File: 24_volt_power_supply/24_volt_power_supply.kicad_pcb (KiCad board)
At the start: 2 copper layers, 75 x 50 mm, 11 parts, among them J1 Conn_01x02_Pin, J2 Screw_Terminal_01x02, J3 Conn_01x02_Pin, K1 Relay_SPDT

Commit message: increased trace thickness for high power
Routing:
- net AC: track 100.7 -> 117.4 mm
- net Net-(J3-Pin_1): track 63.3 -> 65.0 mm
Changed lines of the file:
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@@
 		(start 80.5 71.5)
 		(end 83.5 74.5)
+		(width 3)
+		(layer "F.Cu")
+		(net 3)
+	)
+	(segment
+		(start 92.955113 79.265113)
+		(end 88.19 74.5)
 		(width 0.2)
 		(layer "F.Cu")
@@
 	)
 	(segment
-		(start 125.5 86)
-		(end 130 86)
-		(width 0.2)
-		(layer "F.Cu")
-		(net 3)
-	)
-	(segment
 		(start 87.5 99.5)
 		(end 103.5 99.5)
@@
 	)
 	(segment
-		(start 115 93)
-		(end 118.5 93)
-		(width 0.2)
-		(layer "F.Cu")
-		(net 3)
-	)
-	(segment
 		(start 83.5 95.5)
 		(end 87.5 99.5)
-		(width 0.2)
-		(layer "F.Cu")
-		(net 3)
-	)
-	(segment
-		(start 92.955113 79.265113)
-		(end 88.19 74.5)
-		(width 0.2)
+		(width 3)
 		(layer "F.Cu")
 		(net 3)
@@
 		(start 83.5 74.5)
 		(end 83.5 95.5)
-		(width 0.2)
+		(width 3)
 		(layer "F.Cu")
 		(net 3)
@@
 		(start 103.5 99.5)
 		(end 112.5 90.5)
-		(width 0.2)
-		(layer "F.Cu")
-		(net 3)
-	)
-	(segment
-		(start 118.5 93)
-		(end 125.5 86)
-		(width 0.2)
+		(width 3)
 		(layer "F.Cu")
 		(net 3)
@@
 		(start 76.5 71.5)
 		(end 80.5 71.5)
-		(width 0.2)
+		(width 3)
 		(layer "F.Cu")
 		(net 3)
@@
 	)
 	(segment
-		(start 112.5 90.5)
-		(end 115 93)
-		(width 0.2)
-		(layer "F.Cu")
+		(start 127.5 83.5)
+		(end 130 86)
+		(width 0.2)
+		(layer "B.Cu")
+		(net 3)
+	)
+	(segment
+		(start 92.955113 83.5)
+		(end 127.5 83.5)
+		(width 0.2)
+		(layer "B.Cu")
 		(net 3)
 	)
@@
 		(start 98 80.5)
 		(end 120.5 58)
-		(width 0.2)
+		(width 3)
+		(layer "B.Cu")
+		(net 7)
+	)
+	(segment
+		(start 128.5 56)
+		(end 130.5 58)
+		(width 3)
+		(layer "B.Cu")
+		(net 7)
+	)
+	(segment
+		(start 122.5 56)
+		(end 128.5 56)
+		(width 3)
 		(layer "B.Cu")
 		(net 7)
@@
 	(segment
 		(start 120.5 58)
-		(end 130.5 58)
-		(width 0.2)
+		(end 122.5 56)
+		(width 3)
 		(layer "B.Cu")
 		(net 7)
@@
 		(start 76.5 80.5)
 		(end 98 80.5)
-		(width 0.2)
+		(width 3)
 		(layer "B.Cu")
 		(net 7)
@@
 		(start 132.8 72.2)
 		(end 136.5 72.2)
-		(width 0.2)
+		(width 3)
 		(layer "F.Cu")
 		(net 8)
@@
 		(start 114.5 90.5)
 		(end 132.8 72.2)
-		(width 0.2)
+		(width 3)
 		(layer "F.Cu")
 		(net 8)
@@
 		(start 110.5 89.745)
 		(end 124.5 75.745)
-		(width 0.2)
+		(width 3)
 		(layer "F.Cu")
 		(net 9)
@@
 		(start 124.5 75.745)
 		(end 124.5 72.2)
-		(width 0.2)
+		(width 3)
 		(layer "F.Cu")
 		(net 9)
@@
 		(min_thickness 0.25)
 		(filled_areas_thickness no)
-		(fill yes
+		(fill
 			(thermal_gap 0.5)
 			(thermal_bridge_width 0.5)
@@
 		(polygon
 			(pts
-				(xy 71.5 54.5) (xy 172 54.5) (xy 171.5 154) (xy 71.5 154)
+				(xy 71.5 54.5) (xy 146 55) (xy 146 104.5) (xy 71.5 103.5)
 			)
 		)

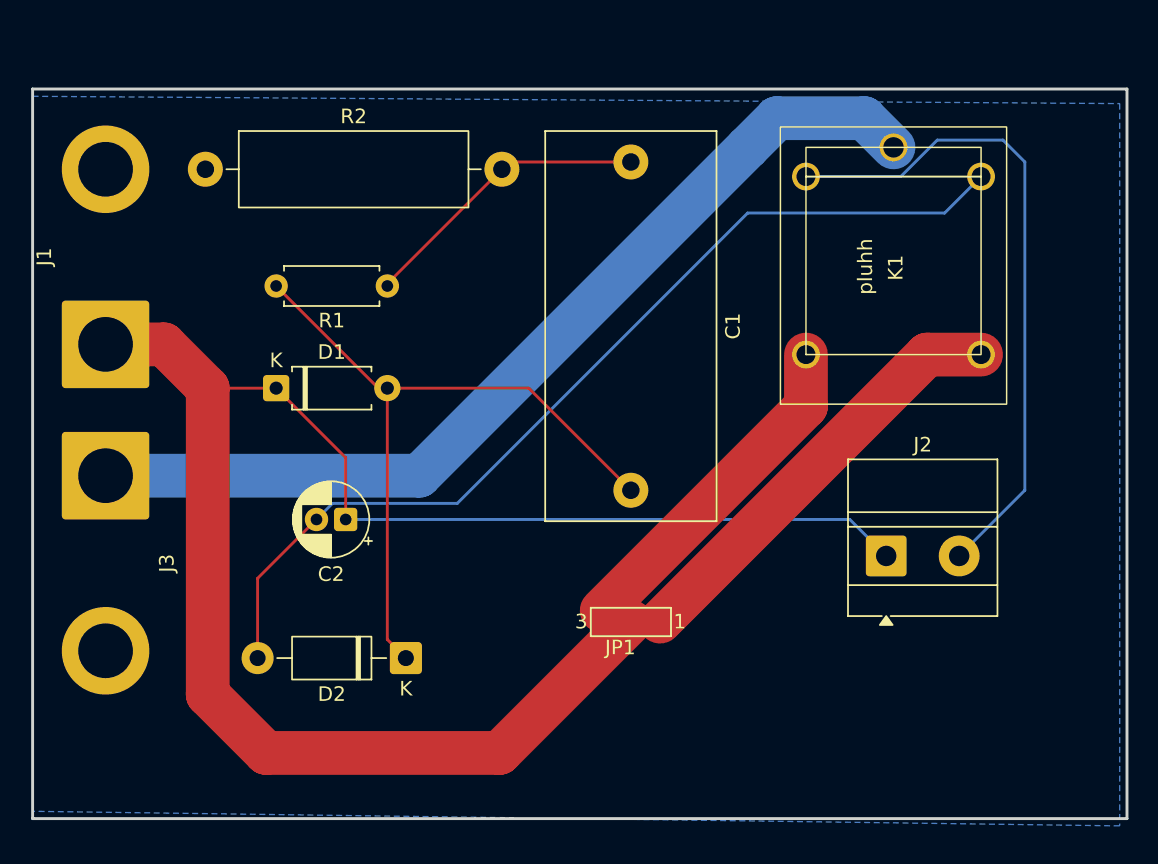
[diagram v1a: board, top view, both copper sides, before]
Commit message: fixed gnd plane issues
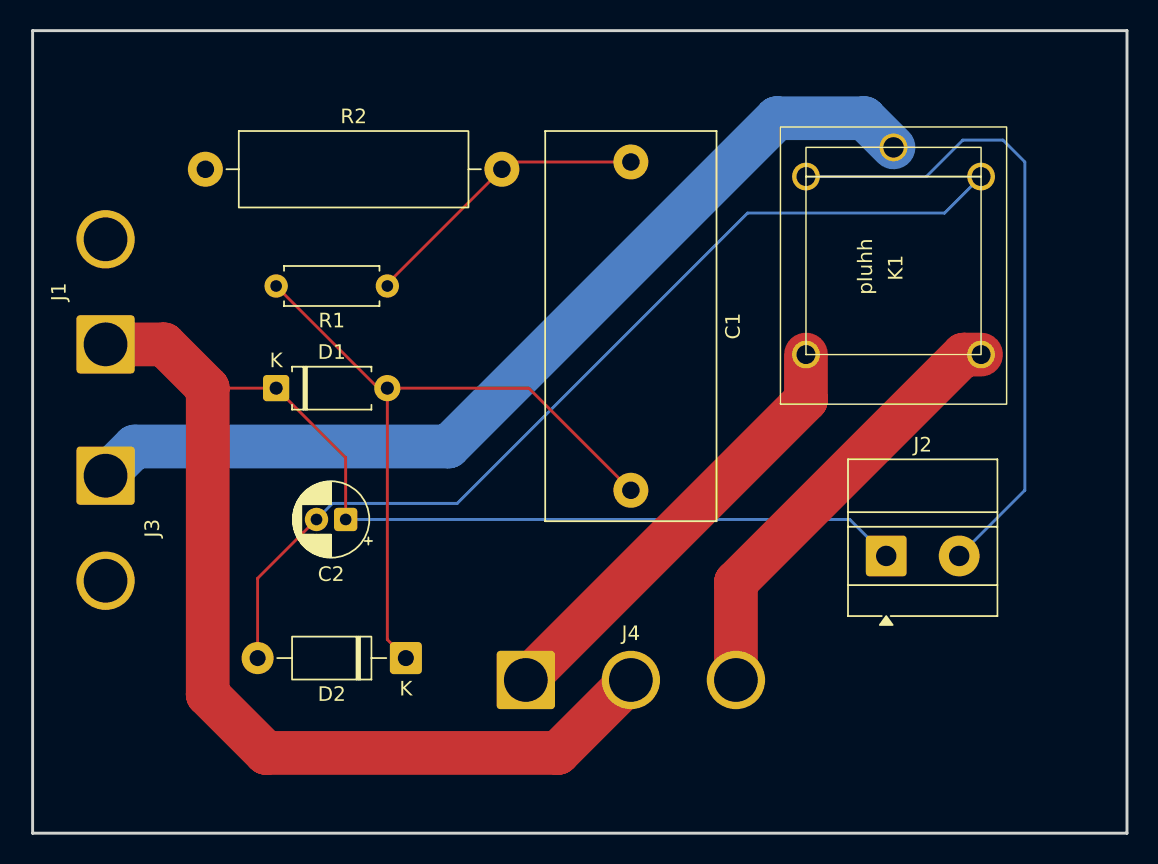
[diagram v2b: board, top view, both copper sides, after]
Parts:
- removed JP1: SolderJumper_3_Open, Jumper:SolderJumper-3_P2.0mm_Open_TrianglePad1.0x1.5mm_NumberLabels
- added J4: Conn_01x03_Pin, Connector_Wire:SolderWire-2.5sqmm_1x03_P7.2mm_D2.4mm_OD3.6mm, F.Cu at (105.3, 94.5)
- J1, J3: footprint Connector_Wire:SolderWire-4sqmm_1x02_P12mm_D3mm_OD6mm -> Connector_Wire:SolderWire-2.5sqmm_1x02_P7.2mm_D2.4mm_OD3.6mm
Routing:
- net Net-(J4-Pin_1): track 24.1 -> 30.3 mm
- net AC: track 117.4 -> 115.7 mm
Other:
- board size 75 x 50 mm -> 75 x 55 mm

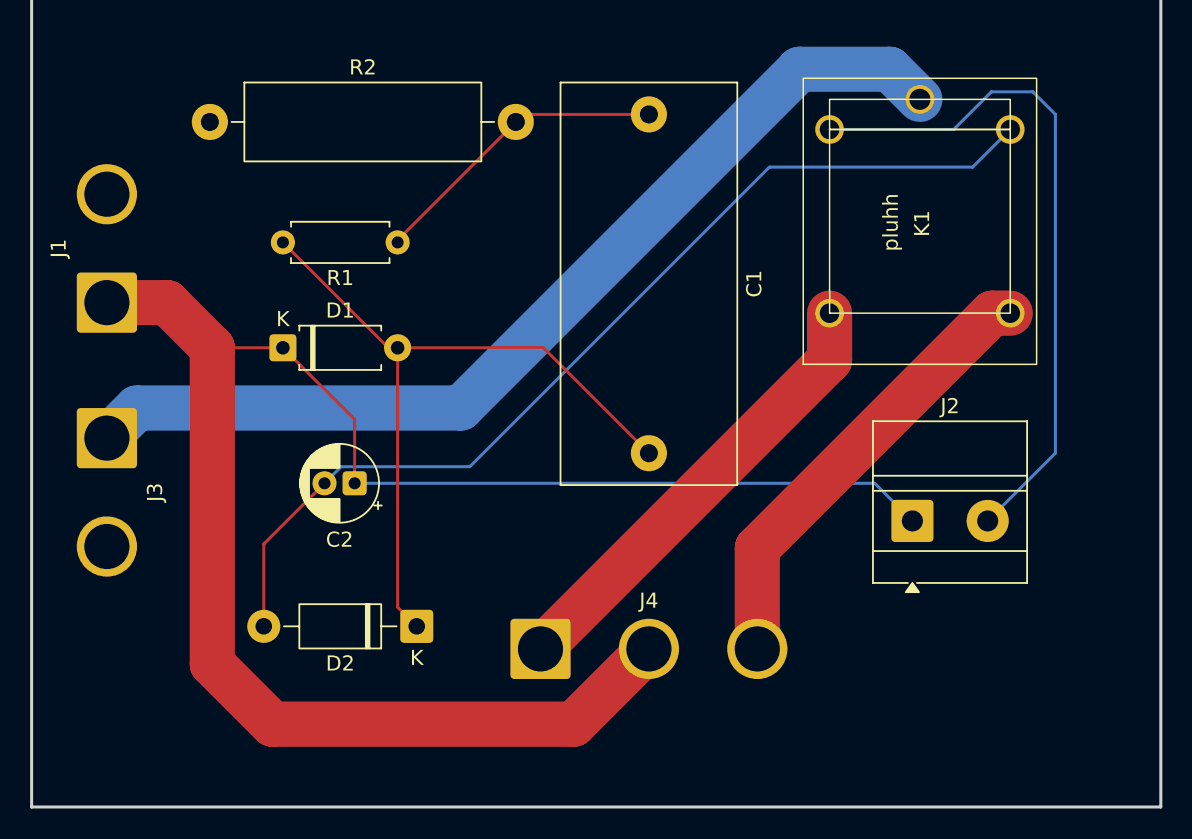
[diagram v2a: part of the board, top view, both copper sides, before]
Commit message: added freewheeling diode
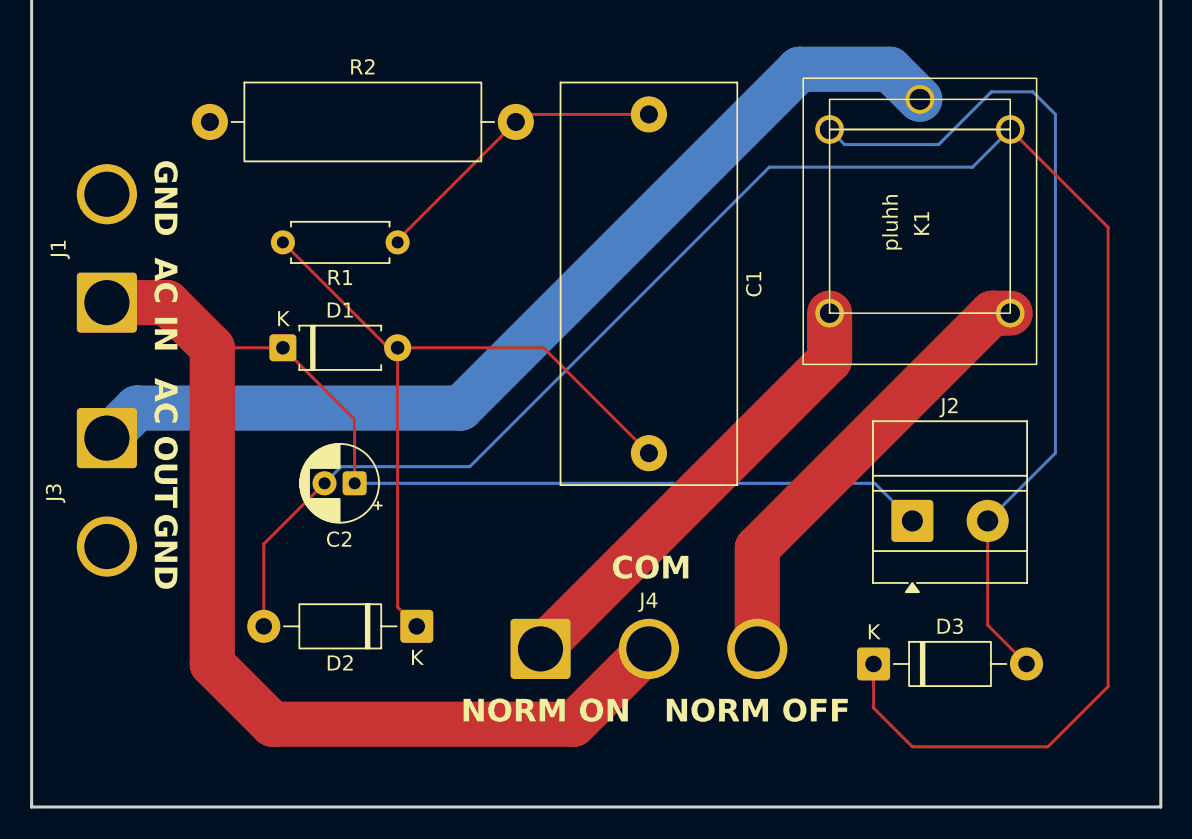
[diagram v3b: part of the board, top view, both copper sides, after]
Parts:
- added D3: 1N4003, Diode_THT:D_DO-41_SOD81_P10.16mm_Horizontal, F.Cu at (127.4, 95.5)
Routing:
- net Net-(D2-A): track 66.5 -> 127.4 mm
- net Net-(D3-A): track 45.5 -> 56.9 mm
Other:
- board text added: "AC IN"
- board text added: "AC OUT"
- board text added: "COM"
- board text added: "GND"
- board text added: "NORM OFF"
- board text added: "NORM ON"

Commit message: updated pcb
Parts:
- moved D3 10.1 mm to (137.5, 95.5), turned to 180 degrees
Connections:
- D3 pad 1: Net-(D2-A) -> Net-(D3-K)
- D3 pad 2: Net-(D3-A) -> Net-(D2-A)
- J2 pad 2: Net-(D3-A) -> Net-(D3-K)
- K1 pad A1: Net-(D3-A) -> Net-(D3-K)
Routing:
- net Net-(D3-K): track 0.00 -> 56.9 mm
- net Net-(D3-A): track 56.9 -> 0.00 mm
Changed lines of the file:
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@@
 	(net 4 "Net-(D2-A)")
 	(net 5 "GND")
-	(net 6 "Net-(D3-A)")
+	(net 6 "Net-(D3-K)")
 	(net 7 "Net-(J3-Pin_1)")
 	(net 8 "Net-(J4-Pin_3)")
@@
 			(layers "*.Cu" "*.Mask")
 			(remove_unused_layers no)
-			(net 6 "Net-(D3-A)")
+			(net 6 "Net-(D3-K)")
 			(pinfunction "Pin_2")
 			(pintype "passive")
@@
 			(layers "*.Cu" "*.Mask")
 			(remove_unused_layers no)
-			(net 6 "Net-(D3-A)")
+			(net 6 "Net-(D3-K)")
 			(pintype "passive")
 		)
@@
 	(footprint "Diode_THT:D_DO-41_SOD81_P10.16mm_Horizontal"
 		(layer "F.Cu")
-		(at 127.42 95.5)
+		(at 137.5 95.5 180)
 		(descr "Diode, DO-41_SOD81 series, Axial, Horizontal, pin pitch=10.16mm, length*diameter=5.2*2.7mm^2, https://www.diodes.com/assets/Package-Files/DO-41-Plastic.pdf")
 		(tags "Diode DO-41_SOD81 series Axial Horizontal pin pitch 10.16mm  length 5.2mm diameter 2.7mm")
@@
 		)
 		(property "Sim.Device" "D"
-			(at 0 0 0)
+			(at 0 0 180)
 			(unlocked yes)
 			(layer "F.Fab")
@@
 		)
 		(property "Sim.Pins" "1=K 2=A"
-			(at 0 0 0)
+			(at 0 0 180)
 			(unlocked yes)
 			(layer "F.Fab")
@@
 		(attr through_hole)
 		(fp_line
-			(start 1.34 0)
-			(end 2.36 0)
+			(start 8.82 0)
+			(end 7.8 0)
 			(stroke
 				(width 0.12)
@@
 		)
 		(fp_line
-			(start 3.14 -1.47)
-			(end 3.14 1.47)
+			(start 3.38 -1.47)
+			(end 3.38 1.47)
 			(stroke
 				(width 0.12)
@@
 		)
 		(fp_line
-			(start 3.38 -1.47)
-			(end 3.38 1.47)
+			(start 3.14 -1.47)
+			(end 3.14 1.47)
 			(stroke
 				(width 0.12)
@@
 		)
 		(fp_line
-			(start 8.82 0)
-			(end 7.8 0)
+			(start 1.34 0)
+			(end 2.36 0)
 			(stroke
 				(width 0.12)
@@
 		)
 		(fp_line
-			(start 0 0)
-			(end 2.48 0)
+			(start 10.16 0)
+			(end 7.68 0)
 			(stroke
 				(width 0.1)
@@
 		)
 		(fp_line
-			(start 3.16 -1.35)
-			(end 3.16 1.35)
+			(start 3.36 -1.35)
+			(end 3.36 1.35)
 			(stroke
 				(width 0.1)
@@
 		)
 		(fp_line
-			(start 3.36 -1.35)
-			(end 3.36 1.35)
+			(start 3.16 -1.35)
+			(end 3.16 1.35)
 			(stroke
 				(width 0.1)
@@
 		)
 		(fp_line
-			(start 10.16 0)
-			(end 7.68 0)
+			(start 0 0)
+			(end 2.48 0)
 			(stroke
 				(width 0.1)
@@
 		)
 		(pad "1" thru_hole roundrect
-			(at 0 0)
+			(at 0 0 180)
 			(size 2.2 2.2)
 			(drill 1.1)
@@
 			(remove_unused_layers no)
 			(roundrect_rratio 0.113636)
-			(net 4 "Net-(D2-A)")
+			(net 6 "Net-(D3-K)")
 			(pinfunction "K")
 			(pintype "passive")
 		)
 		(pad "2" thru_hole circle
-			(at 10.16 0)
+			(at 10.16 0 180)
 			(size 2.2 2.2)
 			(drill 1.1)
 			(layers "*.Cu" "*.Mask")
 			(remove_unused_layers no)
-			(net 6 "Net-(D3-A)")
+			(net 4 "Net-(D2-A)")
 			(pinfunction "A")
 			(pintype "passive")

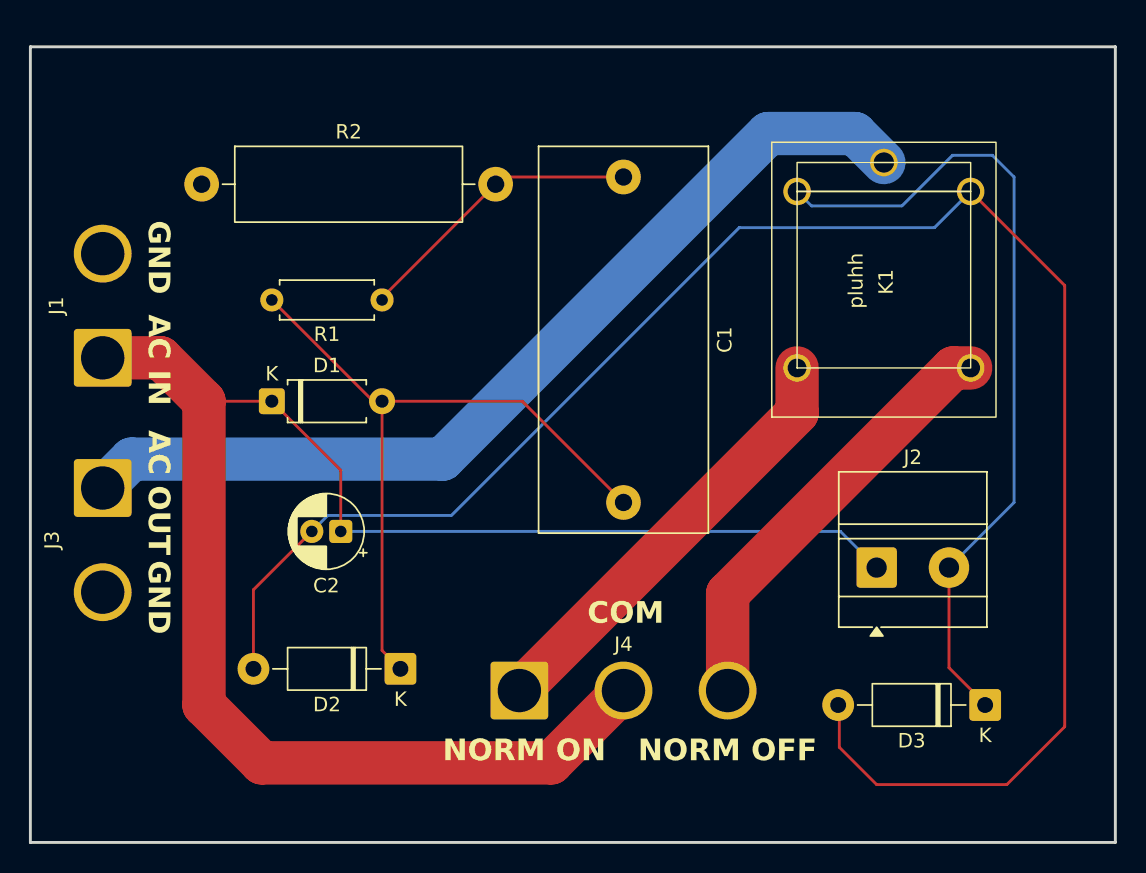
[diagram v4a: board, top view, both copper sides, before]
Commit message: started mounting holes for pcb
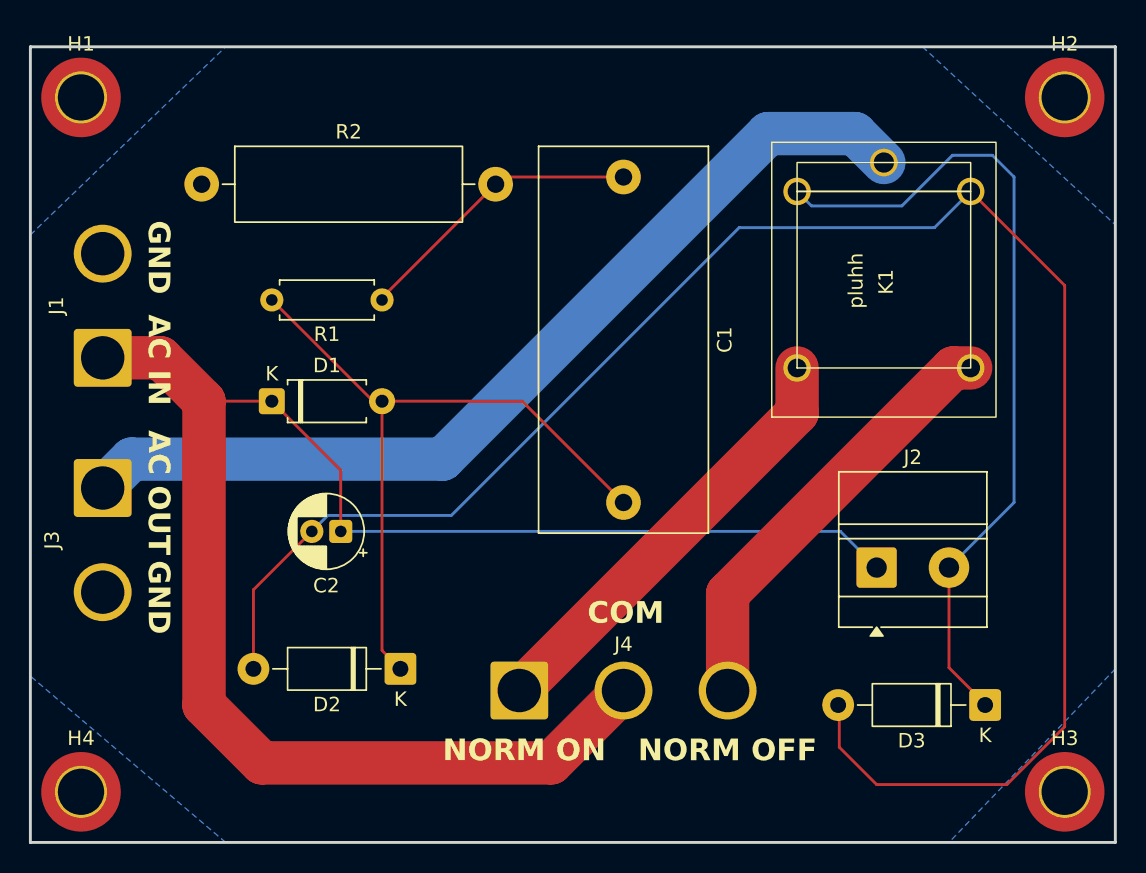
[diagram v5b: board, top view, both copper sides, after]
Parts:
- added H1: MountingHole, MountingHole:MountingHole_3.2mm_M3_ISO14580_Pad_TopOnly, F.Cu at (75.0, 53.5)
- added H2: MountingHole, MountingHole:MountingHole_3.2mm_M3_ISO14580_Pad_TopOnly, F.Cu at (143.0, 53.5)
- added H3: MountingHole, MountingHole:MountingHole_3.2mm_M3_ISO14580_Pad_TopOnly, F.Cu at (143.0, 101.5)
- added H4: MountingHole, MountingHole:MountingHole_3.2mm_M3_ISO14580_Pad_TopOnly, F.Cu at (75.0, 101.5)
